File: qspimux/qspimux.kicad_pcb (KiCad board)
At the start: 2 copper layers, 24.8 x 13.8 mm, 15 parts, among them J101 Conn_02x05_Odd_Even, J102 Conn_02x04_Odd_Even, J103 Conn_02x04_Odd_Even, Q101 PMV50XP, Q102 PMV50XP, U101 TS3A27518ERTWR

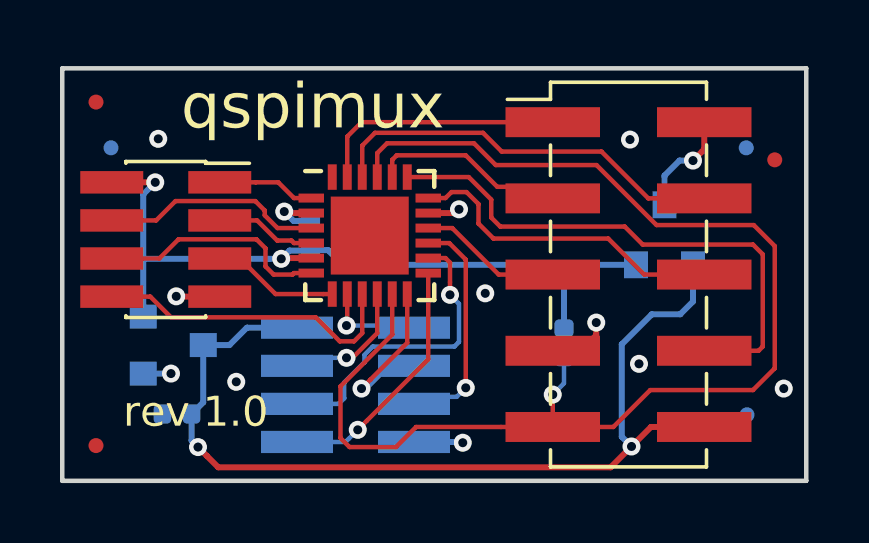
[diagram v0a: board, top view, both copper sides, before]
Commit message: fix mirrored footprints in qspimux design
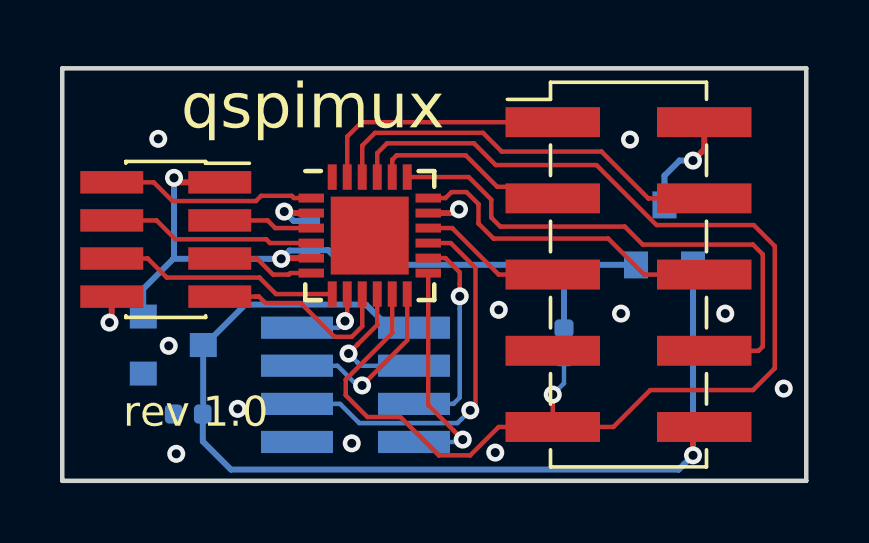
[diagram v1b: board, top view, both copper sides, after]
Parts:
- removed REF** (x6): Fiducial_0.5mm_Dia_1mm_Outer, Fiducial:Fiducial_0.5mm_Dia_1mm_Outer
- moved R102 0.38 mm to (95.0, 97.8)
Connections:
- J102 pad 1: /~CS_FLASH -> /VCC_FLASH
- J102 pad 2: /VCC_FLASH -> /~CS_FLASH
- J102 pad 3: /IO0_DO_FLASH -> /IO3_~HOLD_FLASH
- J102 pad 4: /IO3_~HOLD_FLASH -> /IO0_DO_FLASH
- J102 pad 5: /IO2_~WP_FLASH -> /CLK_FLASH
- J102 pad 6: /CLK_FLASH -> /IO2_~WP_FLASH
- J102 pad 7: GND -> /IO0_DI_FLASH
- J102 pad 8: /IO0_DI_FLASH -> GND
- J103 pad 1: /~CS_BOARD -> /VCC_BOARD
- J103 pad 2: /VCC_BOARD -> /~CS_BOARD
- J103 pad 3: /IO0_DO_BOARD -> /IO3_~HOLD_BOARD
- J103 pad 4: /IO3_~HOLD_BOARD -> /IO0_DO_BOARD
- J103 pad 5: /IO2_~WP_BOARD -> /CLK_BOARD
- J103 pad 6: /CLK_BOARD -> /IO2_~WP_BOARD
- J103 pad 7: GND -> /IO0_DI_BOARD
- J103 pad 8: /IO0_DI_BOARD -> GND
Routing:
- net /IO2_~WP_BOARD: track 7.70 -> 13.0 mm
- net GND: track 9.11 -> 3.90 mm, vias 12 -> 14
- net /CLK_FLASH: track 7.78 -> 3.29 mm
- net /IO3_~HOLD_FLASH: track 7.38 -> 3.16 mm
- net /IO0_DI_FLASH: track 10.4 -> 6.53 mm
- net /~CS_FLASH: track 3.27 -> 7.01 mm
- net /IO2_~WP_FLASH: track 4.24 -> 7.84 mm
- net /IO0_DO_FLASH: track 3.36 -> 6.96 mm
- net /CLK_BOARD: track 10.3 -> 7.03 mm
- net /VCC_BOARD: track 32.5 -> 35.6 mm, vias 2 -> 1
- net /MUX_SEL: track 43.4 -> 42.5 mm
- net /~CS_BOARD: track 3.34 -> 2.62 mm
- net /IO0_DI_BOARD: track 8.39 -> 7.68 mm
